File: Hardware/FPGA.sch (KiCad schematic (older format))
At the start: 17 parts, among them U501 W25Q128JVxxM, U502 ICE40UP5K-SG48, U503 Crystal Oscillator, U504 USBLC6-2

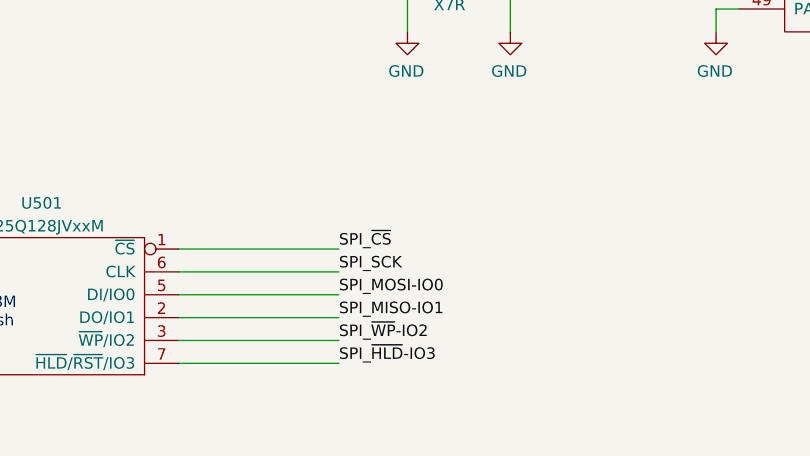
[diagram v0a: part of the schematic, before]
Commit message: Connecting up SAO.
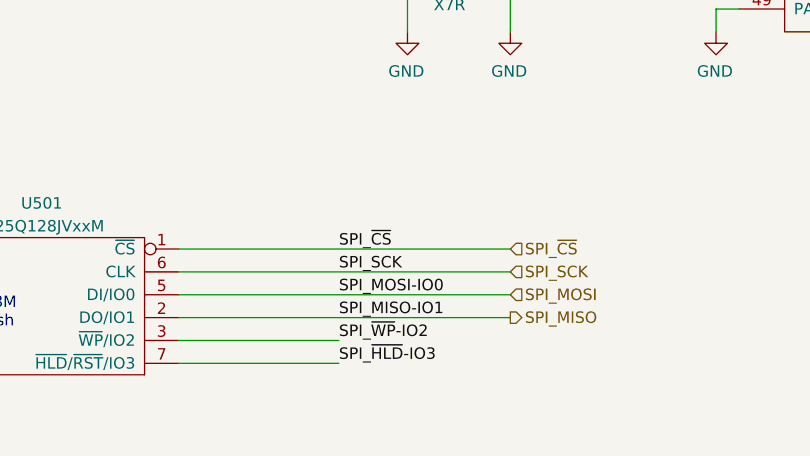
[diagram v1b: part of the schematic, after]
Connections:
- net labels added: SPI_MISO, SPI_MOSI
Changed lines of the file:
@@
 $Descr A4 11693 8268
 encoding utf-8
-Sheet 5 9
+Sheet 5 7
 Title ""
 Date ""
@@
 Wire Wire Line
 	3000 6500 3700 6500
-Wire Wire Line
-	3000 6200 3700 6200
-Wire Wire Line
-	3000 6100 3700 6100
-Wire Wire Line
-	3000 6300 3700 6300
-Wire Wire Line
-	3000 6400 3700 6400
 Wire Wire Line
 	3000 6600 3700 6600
@@
 Wire Wire Line
 	7450 1950 8000 1950
+Text HLabel 4450 6100 2    50   Input ~ 0
+SPI_~CS
+Text HLabel 4450 6200 2    50   Input ~ 0
+SPI_SCK
+Text HLabel 4450 6300 2    50   Input ~ 0
+SPI_MOSI
+Text HLabel 4450 6400 2    50   Output ~ 0
+SPI_MISO
+Wire Wire Line
+	3000 6400 4450 6400
+Wire Wire Line
+	3000 6300 4450 6300
+Wire Wire Line
+	3000 6200 4450 6200
+Wire Wire Line
+	3000 6100 4450 6100
 $EndSCHEMATC

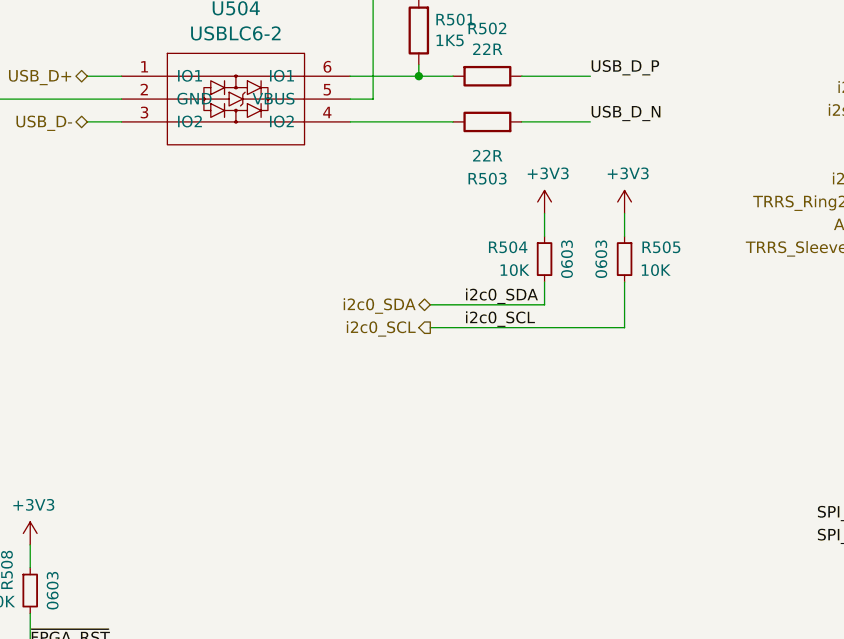
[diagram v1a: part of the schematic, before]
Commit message: Commit before branch to fix VIN=3v3 from SAO.
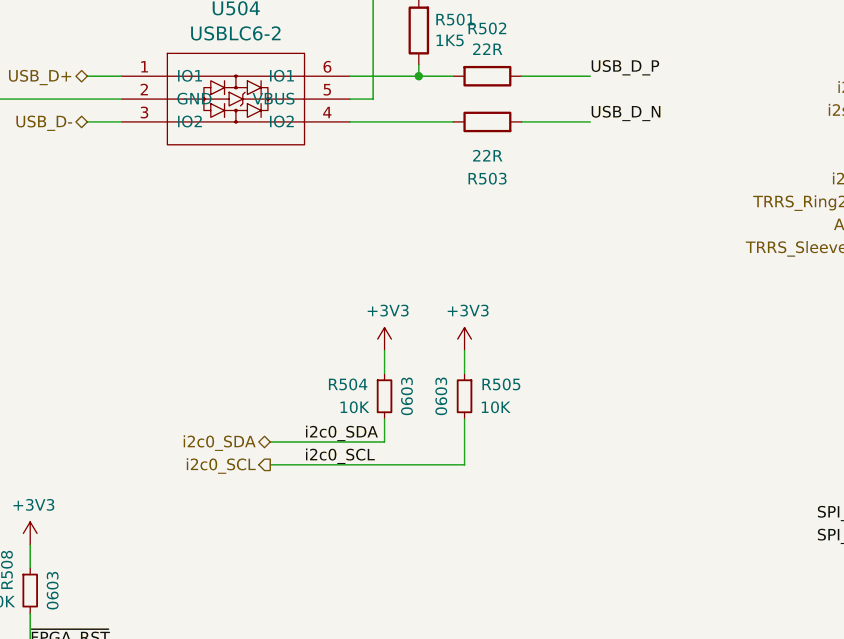
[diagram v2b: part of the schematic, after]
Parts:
- U501: DPN W25Q128JVPIMCT-ND -> W25Q128JVPIQ-ND; MPN W25Q128JVPIM TR -> W25Q128JVPIQ
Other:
- moved on the sheet: R504, R505
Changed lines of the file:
@@
 Wire Wire Line
 	7450 3050 8000 3050
-Text HLabel 3200 2400 0    50   BiDi ~ 0
+Text HLabel 2500 3000 0    50   BiDi ~ 0
 i2c0_SDA
-Text HLabel 3200 2500 0    50   Output ~ 0
+Text HLabel 2500 3100 0    50   Output ~ 0
 i2c0_SCL
 Text HLabel 8000 1650 2    50   Output ~ 0
@@
 F 4 "ANY" H 2400 6300 50  0001 C CNN "Source"
 F 5 "eeprom-wson8-w25q128" H -5500 -1650 50  0001 C CNN "Key"
-F 6 "W25Q128JVPIM TR" H 2400 6300 50  0001 C CNN "MPN"
-F 7 "W25Q128JVPIMCT-ND" H 2400 6300 50  0001 C CNN "DPN"
+F 6 "W25Q128JVPIQ" H 2400 6300 50  0001 C CNN "MPN"
+F 7 "W25Q128JVPIQ-ND" H 2400 6300 50  0001 C CNN "DPN"
 	1    2400 6300
 	-1   0    0    -1
@@
 L Device:R_Small R?
 U 1 1 61550D45
-P 3700 2200
+P 3000 2800
 AR Path="/611E335F/61550D45" Ref="R?"  Part="1"
 AR Path="/61550D45" Ref="R?"  Part="1"
 AR Path="/611E3335/61550D45" Ref="R504"  Part="1"
-F 0 "R504" H 3450 2250 50  0000 L CNN
-F 1 "10K" H 3500 2150 50  0000 L CNN
-F 2 "Resistor_SMD:R_0603_1608Metric" V 3630 2200 50  0001 C CNN
-F 3 "~" H 3700 2200 50  0001 C CNN
-F 4 "0603" V 3800 2200 50  0000 C CNN "Pkg"
-F 5 "RNCP0603FTD10K0" H 3700 2200 50  0001 C CNN "MPN"
-F 6 "RNCP0603FTD10K0CT-ND" H 3700 2200 50  0001 C CNN "DPN"
-	1    3700 2200
+F 0 "R504" H 2750 2850 50  0000 L CNN
+F 1 "10K" H 2800 2750 50  0000 L CNN
+F 2 "Resistor_SMD:R_0603_1608Metric" V 2930 2800 50  0001 C CNN
+F 3 "~" H 3000 2800 50  0001 C CNN
+F 4 "0603" V 3100 2800 50  0000 C CNN "Pkg"
+F 5 "RNCP0603FTD10K0" H 3000 2800 50  0001 C CNN "MPN"
+F 6 "RNCP0603FTD10K0CT-ND" H 3000 2800 50  0001 C CNN "DPN"
+	1    3000 2800
 	1    0    0    -1
 $EndComp
@@
 L Device:R_Small R?
 U 1 1 6155177C
-P 4050 2200
+P 3350 2800
 AR Path="/611E335F/6155177C" Ref="R?"  Part="1"
 AR Path="/6155177C" Ref="R?"  Part="1"
 AR Path="/611E3335/6155177C" Ref="R505"  Part="1"
-F 0 "R505" H 3800 2250 50  0000 L CNN
-F 1 "10K" H 3850 2150 50  0000 L CNN
-F 2 "Resistor_SMD:R_0603_1608Metric" V 3980 2200 50  0001 C CNN
-F 3 "~" H 4050 2200 50  0001 C CNN
-F 4 "0603" V 4150 2200 50  0000 C CNN "Pkg"
-F 5 "RNCP0603FTD10K0" H 4050 2200 50  0001 C CNN "MPN"
-F 6 "RNCP0603FTD10K0CT-ND" H 4050 2200 50  0001 C CNN "DPN"
-	1    4050 2200
+F 0 "R505" H 3100 2850 50  0000 L CNN
+F 1 "10K" H 3150 2750 50  0000 L CNN
+F 2 "Resistor_SMD:R_0603_1608Metric" V 3280 2800 50  0001 C CNN
+F 3 "~" H 3350 2800 50  0001 C CNN
+F 4 "0603" V 3450 2800 50  0000 C CNN "Pkg"
+F 5 "RNCP0603FTD10K0" H 3350 2800 50  0001 C CNN "MPN"
+F 6 "RNCP0603FTD10K0CT-ND" H 3350 2800 50  0001 C CNN "DPN"
+	1    3350 2800
 	-1   0    0    -1
 $EndComp
@@
 L power:+3V3 #PWR0141
 U 1 1 61554096
-P 3700 2000
-F 0 "#PWR0141" H 3700 1850 50  0001 C CNN
-F 1 "+3V3" H 3715 2173 50  0000 C CNN
-F 2 "" H 3700 2000 50  0001 C CNN
-F 3 "" H 3700 2000 50  0001 C CNN
-	1    3700 2000
+P 3000 2600
+F 0 "#PWR0141" H 3000 2450 50  0001 C CNN
+F 1 "+3V3" H 3015 2773 50  0000 C CNN
+F 2 "" H 3000 2600 50  0001 C CNN
+F 3 "" H 3000 2600 50  0001 C CNN
+	1    3000 2600
 	1    0    0    -1
 $EndComp
@@
 L power:+3V3 #PWR0142
 U 1 1 615544FD
-P 4050 2000
-F 0 "#PWR0142" H 4050 1850 50  0001 C CNN
-F 1 "+3V3" H 4065 2173 50  0000 C CNN
-F 2 "" H 4050 2000 50  0001 C CNN
-F 3 "" H 4050 2000 50  0001 C CNN
-	1    4050 2000
-	1    0    0    -1
-$EndComp
-Wire Wire Line
-	3700 2000 3700 2100
-Wire Wire Line
-	4050 2000 4050 2100
-Wire Wire Line
-	3700 2300 3700 2400
-Wire Wire Line
-	3700 2400 3200 2400
-Wire Wire Line
-	4050 2300 4050 2500
-Wire Wire Line
-	4050 2500 3200 2500
+P 3350 2600
+F 0 "#PWR0142" H 3350 2450 50  0001 C CNN
+F 1 "+3V3" H 3365 2773 50  0000 C CNN
+F 2 "" H 3350 2600 50  0001 C CNN
+F 3 "" H 3350 2600 50  0001 C CNN
+	1    3350 2600
+	1    0    0    -1
+$EndComp
+Wire Wire Line
+	3000 2600 3000 2700
+Wire Wire Line
+	3350 2600 3350 2700
+Wire Wire Line
+	3000 2900 3000 3000
+Wire Wire Line
+	3000 3000 2500 3000
+Wire Wire Line
+	3350 2900 3350 3100
+Wire Wire Line
+	3350 3100 2500 3100
 $Comp
 L Device:R_Small R?
@@
 Wire Wire Line
 	5350 1850 5450 1850
-Text Label 3350 2400 0    50   ~ 0
+Text Label 2650 3000 0    50   ~ 0
 i2c0_SDA
-Text Label 3350 2500 0    50   ~ 0
+Text Label 2650 3100 0    50   ~ 0
 i2c0_SCL
 Wire Wire Line

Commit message: Commit berfore merge back with power fix.
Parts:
- removed R504, R505: 10K, Resistor_SMD:R_0603_1608Metric, symbol Device:R_Small
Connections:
- wire segments 94 -> 88
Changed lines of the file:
@@
 Wire Wire Line
 	7450 3050 8000 3050
-Text HLabel 2500 3000 0    50   BiDi ~ 0
+Text HLabel 1250 2900 0    50   BiDi ~ 0
 i2c0_SDA
-Text HLabel 2500 3100 0    50   Output ~ 0
+Text HLabel 1250 3000 0    50   Output ~ 0
 i2c0_SCL
 Text HLabel 8000 1650 2    50   Output ~ 0
@@
 Text Label 3900 1600 0    50   ~ 0
 USB_D_N
-$Comp
-L Device:R_Small R?
-U 1 1 61550D45
-P 3000 2800
-AR Path="/611E335F/61550D45" Ref="R?"  Part="1"
-AR Path="/61550D45" Ref="R?"  Part="1"
-AR Path="/611E3335/61550D45" Ref="R504"  Part="1"
-F 0 "R504" H 2750 2850 50  0000 L CNN
-F 1 "10K" H 2800 2750 50  0000 L CNN
-F 2 "Resistor_SMD:R_0603_1608Metric" V 2930 2800 50  0001 C CNN
-F 3 "~" H 3000 2800 50  0001 C CNN
-F 4 "0603" V 3100 2800 50  0000 C CNN "Pkg"
-F 5 "RNCP0603FTD10K0" H 3000 2800 50  0001 C CNN "MPN"
-F 6 "RNCP0603FTD10K0CT-ND" H 3000 2800 50  0001 C CNN "DPN"
-	1    3000 2800
-	1    0    0    -1
-$EndComp
-$Comp
-L Device:R_Small R?
-U 1 1 6155177C
-P 3350 2800
-AR Path="/611E335F/6155177C" Ref="R?"  Part="1"
-AR Path="/6155177C" Ref="R?"  Part="1"
-AR Path="/611E3335/6155177C" Ref="R505"  Part="1"
-F 0 "R505" H 3100 2850 50  0000 L CNN
-F 1 "10K" H 3150 2750 50  0000 L CNN
-F 2 "Resistor_SMD:R_0603_1608Metric" V 3280 2800 50  0001 C CNN
-F 3 "~" H 3350 2800 50  0001 C CNN
-F 4 "0603" V 3450 2800 50  0000 C CNN "Pkg"
-F 5 "RNCP0603FTD10K0" H 3350 2800 50  0001 C CNN "MPN"
-F 6 "RNCP0603FTD10K0CT-ND" H 3350 2800 50  0001 C CNN "DPN"
-	1    3350 2800
-	-1   0    0    -1
-$EndComp
-$Comp
-L power:+3V3 #PWR0141
-U 1 1 61554096
-P 3000 2600
-F 0 "#PWR0141" H 3000 2450 50  0001 C CNN
-F 1 "+3V3" H 3015 2773 50  0000 C CNN
-F 2 "" H 3000 2600 50  0001 C CNN
-F 3 "" H 3000 2600 50  0001 C CNN
-	1    3000 2600
-	1    0    0    -1
-$EndComp
-$Comp
-L power:+3V3 #PWR0142
-U 1 1 615544FD
-P 3350 2600
-F 0 "#PWR0142" H 3350 2450 50  0001 C CNN
-F 1 "+3V3" H 3365 2773 50  0000 C CNN
-F 2 "" H 3350 2600 50  0001 C CNN
-F 3 "" H 3350 2600 50  0001 C CNN
-	1    3350 2600
-	1    0    0    -1
-$EndComp
-Wire Wire Line
-	3000 2600 3000 2700
-Wire Wire Line
-	3350 2600 3350 2700
-Wire Wire Line
-	3000 2900 3000 3000
-Wire Wire Line
-	3000 3000 2500 3000
-Wire Wire Line
-	3350 2900 3350 3100
-Wire Wire Line
-	3350 3100 2500 3100
+Wire Wire Line
+	1750 2900 1250 2900
+Wire Wire Line
+	1750 3000 1250 3000
 $Comp
 L Device:R_Small R?
@@
 Text HLabel 5350 2050 0    50   Output ~ 0
 AMP_VOL
-Wire Wire Line
-	8950 5150 8850 5150
 Text HLabel 8000 3450 2    50   Output ~ 0
 AMP_PL
-Wire Wire Line
-	8950 5000 8850 5000
 $Comp
 L Device:R_Small R?
@@
 Wire Wire Line
 	5350 1850 5450 1850
-Text Label 2650 3000 0    50   ~ 0
+Text Label 1400 2900 0    50   ~ 0
 i2c0_SDA
-Text Label 2650 3100 0    50   ~ 0
+Text Label 1400 3000 0    50   ~ 0
 i2c0_SCL
 Wire Wire Line

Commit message: Placements mostly done.
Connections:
- wire segments 88 -> 91
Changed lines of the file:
@@
 Text HLabel 8000 1650 2    50   Output ~ 0
 DAC_Latch
-Text HLabel 8000 2450 2    50   Output ~ 0
+Text HLabel 8000 2250 2    50   Output ~ 0
 VO_VOLUME
 Text HLabel 8000 4050 2    50   Output ~ 0
@@
 F 7 "1269406" H 2350 1500 50  0001 C CNN "E14PN"
 	1    2350 1500
-	1    0    0    -1
+	1    0    0    1
 $EndComp
 Text HLabel 1300 4250 0    50   Input ~ 0
@@
 	8000 4050 7450 4050
 Wire Wire Line
-	8000 2450 7450 2450
+	8000 2250 7450 2250
 Wire Wire Line
 	8000 1650 7450 1650
@@
 Wire Wire Line
 	3000 6100 4450 6100
+Wire Wire Line
+	1300 4250 1400 4250
+Wire Wire Line
+	1300 4550 1400 4550
+Wire Wire Line
+	1300 4700 1400 4700
 $EndSCHEMATC

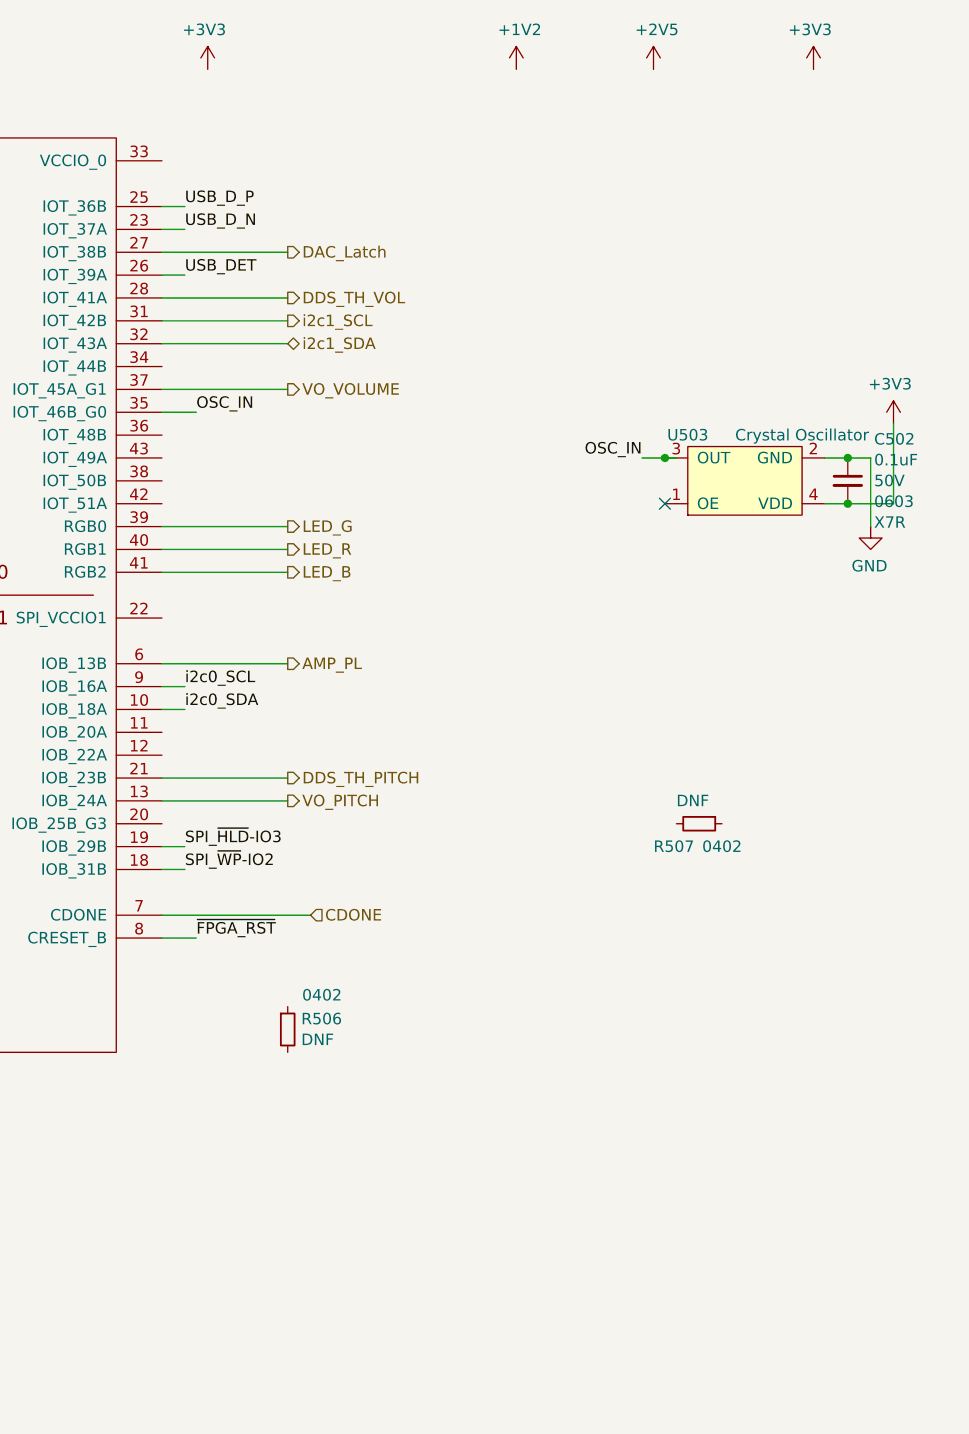
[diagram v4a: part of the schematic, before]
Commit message: Most placements, testpoints and spare points added. Looking good.
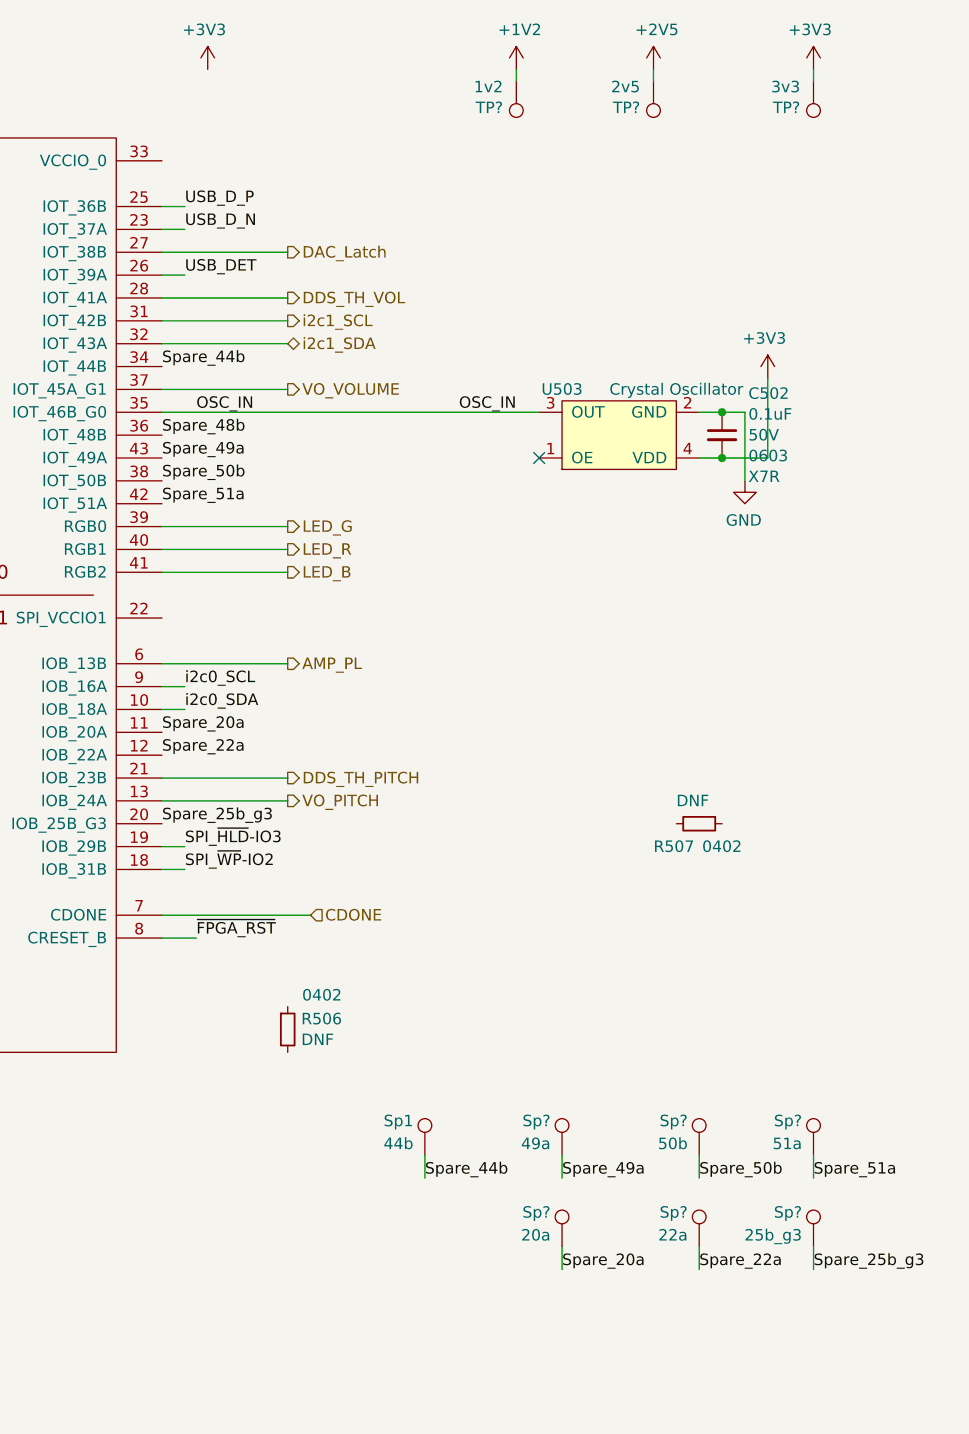
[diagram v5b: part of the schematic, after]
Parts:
- added Sp1: 44b, TestPoint:TestPoint_THTPad_D2.5mm_Drill1.2mm, symbol OpenThereminCC-rescue:TEST_1P
- added Sp?: 49a, TestPoint:TestPoint_THTPad_D2.5mm_Drill1.2mm, symbol OpenThereminCC-rescue:TEST_1P
- added Sp?: 50b, TestPoint:TestPoint_THTPad_D2.5mm_Drill1.2mm, symbol OpenThereminCC-rescue:TEST_1P
- added Sp?: 51a, TestPoint:TestPoint_THTPad_D2.5mm_Drill1.2mm, symbol OpenThereminCC-rescue:TEST_1P
- added Sp?: 20a, TestPoint:TestPoint_THTPad_D2.5mm_Drill1.2mm, symbol OpenThereminCC-rescue:TEST_1P
- added Sp?: 22a, TestPoint:TestPoint_THTPad_D2.5mm_Drill1.2mm, symbol OpenThereminCC-rescue:TEST_1P
- added Sp?: 25b_g3, TestPoint:TestPoint_THTPad_D2.5mm_Drill1.2mm, symbol OpenThereminCC-rescue:TEST_1P
- added TP?: 1v2, TestPoint:TestPoint_THTPad_D1.5mm_Drill0.7mm, symbol Connector:TestPoint
- added TP?: 2v5, TestPoint:TestPoint_THTPad_D1.5mm_Drill0.7mm, symbol Connector:TestPoint
- added TP?: 3v3, TestPoint:TestPoint_THTPad_D1.5mm_Drill0.7mm, symbol Connector:TestPoint
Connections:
- net +1V2: now also TP?.1
- net +2V5: now also TP?.1
- net +3V3: now also TP?.1
- net Spare_20a: now reaches U502.11 (IOB_20A)
- net Spare_20a: now also Sp?.1
- net Spare_22a: now reaches U502.12 (IOB_22A)
- net Spare_22a: now also Sp?.1
- net Spare_25b_g3: now reaches U502.20 (IOB_25B_G3)
- net Spare_25b_g3: now also Sp?.1
- net Spare_44b: now reaches U502.34 (IOT_44B)
- net Spare_44b: now also Sp1.1
- net Spare_48b: now reaches U502.36 (IOT_48B)
- net Spare_50b: now reaches U502.38 (IOT_50B)
- net Spare_50b: now also Sp?.1
- net Spare_51a: now reaches U502.42 (IOT_51A)
- net Spare_51a: now also Sp?.1
- net Spare_49a: now reaches U502.43 (IOT_49A)
- net Spare_49a: now also Sp?.1
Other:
- moved on the sheet: C502, U503
